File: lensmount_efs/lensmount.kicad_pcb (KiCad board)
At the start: 2 copper layers, 49.8 x 49.8 mm, 39 parts, among them J1 VBAT, J10 Picoblade DNP, J2 DETECT, J3 AGND, J4 VDD, J5 DOUT, J6 DIN, J7 DCLK, J8 DGND, P1 TC2030-CTX-Tag-Connect, Q1 2N7002, Q2 2N7002, Q3 2N7002, Q4 AO3401A, Q5 AO3401A, U1 STM32F042G6Ux, U2 XC6206PxxxMR

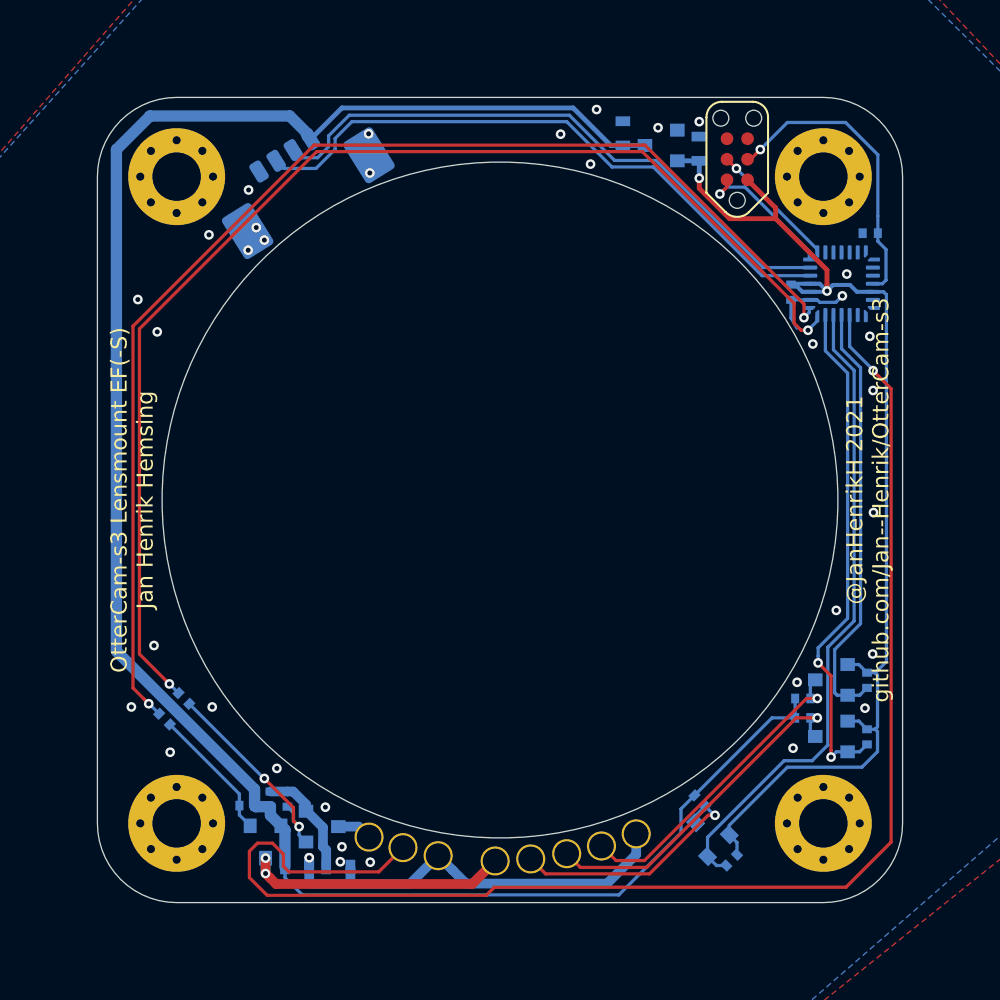
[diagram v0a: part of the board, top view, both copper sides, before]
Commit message: updated to kicad 6
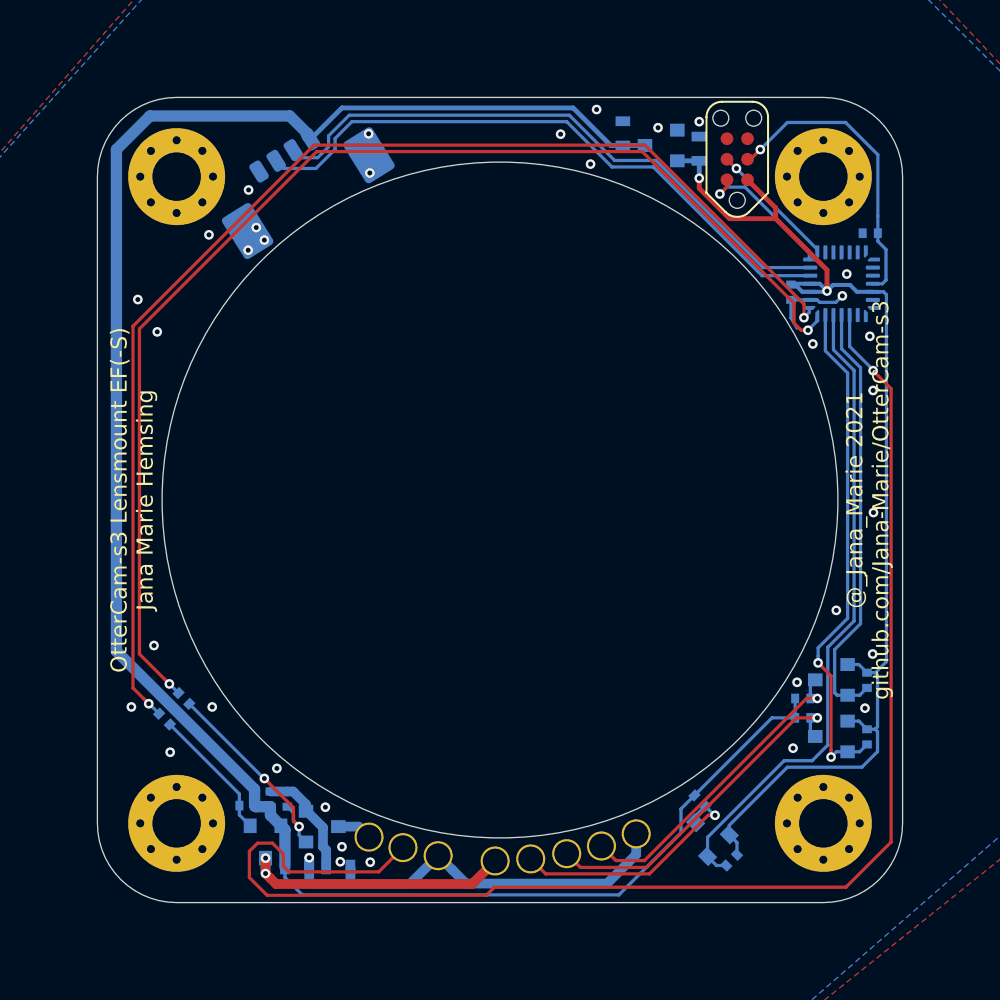
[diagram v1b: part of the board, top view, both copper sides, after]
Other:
- net class Default removed
- board text added: "@_Jana_Marie 2021 github.com/Jana-Marie/OtterCam-s3"
- board text added: "OtterCam-s3 Lensmount EF(-S) Jana Marie Hemsing"
- board text removed: "@JanHenrikH 2021 github.com/Jan--Henrik/OtterCam-s3"
- board text removed: "OtterCam-s3 Lensmount EF(-S) Jan Henrik Hemsing"

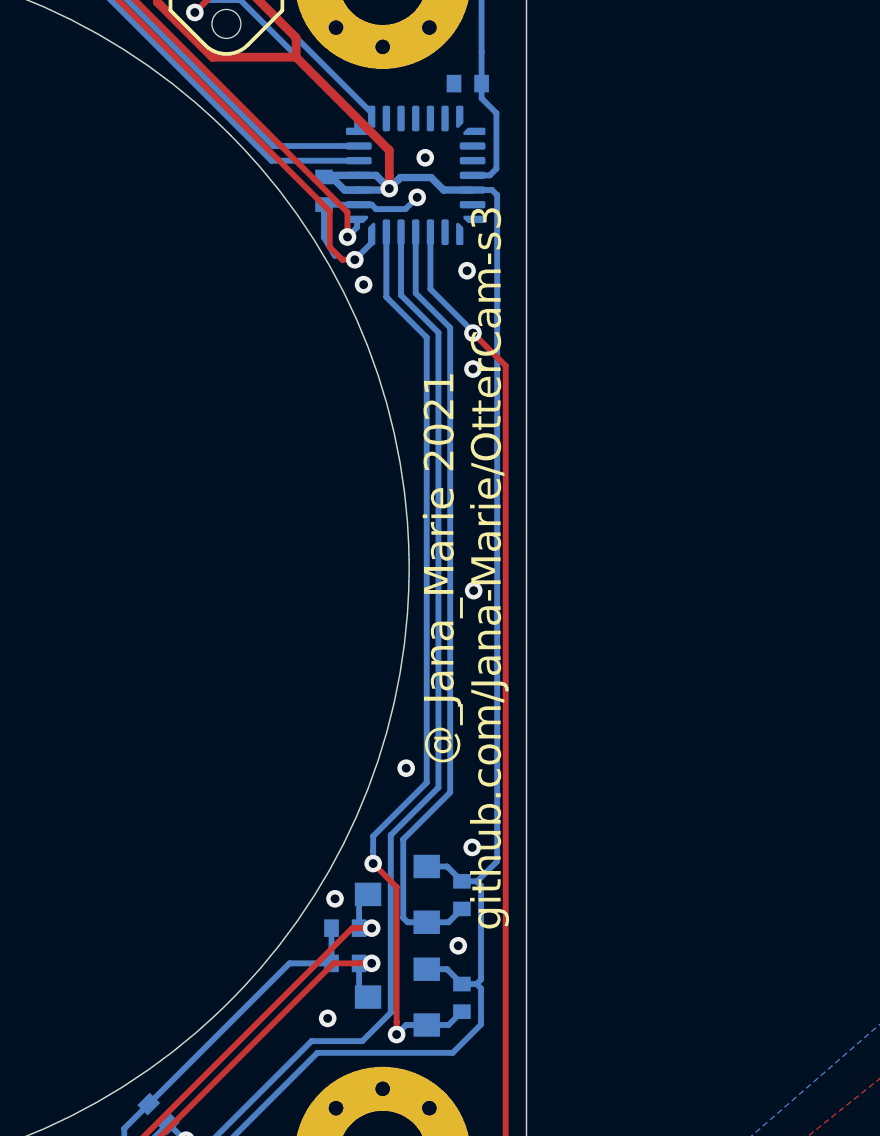
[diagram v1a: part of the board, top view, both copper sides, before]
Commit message: updated lensmount
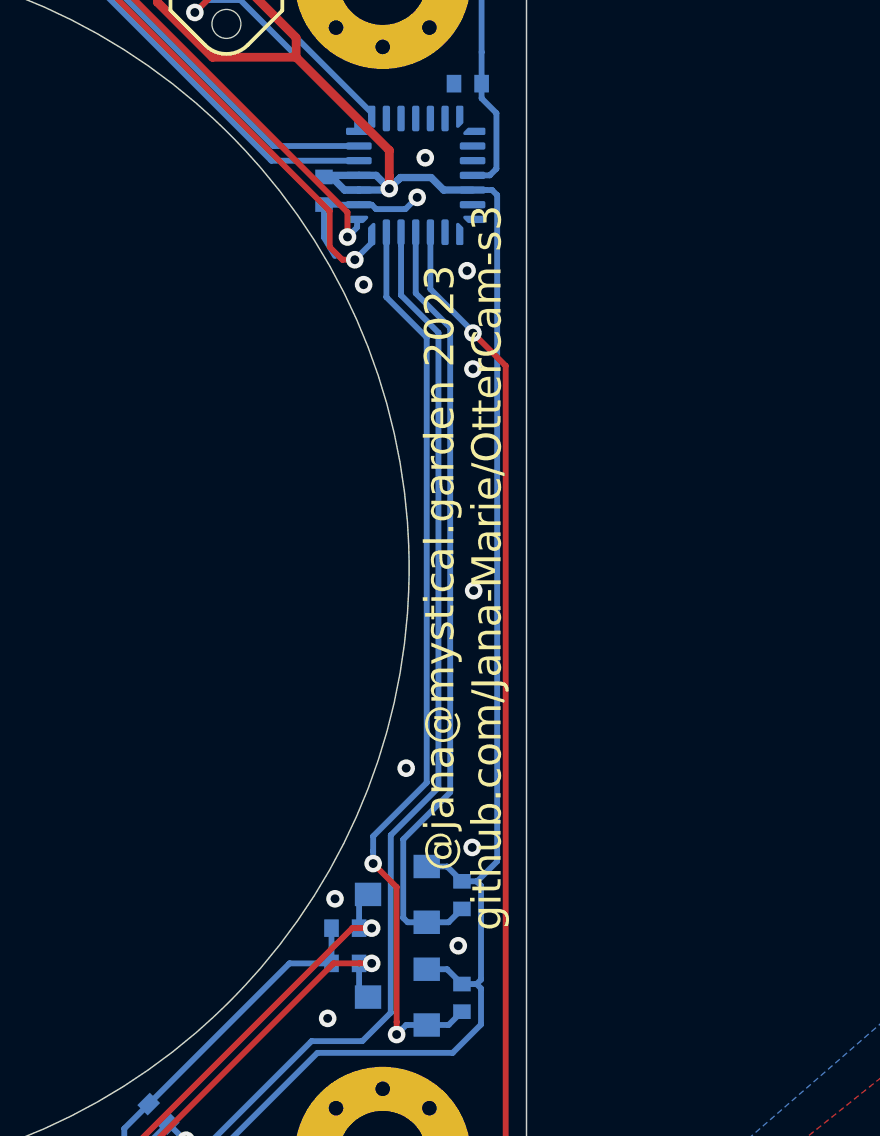
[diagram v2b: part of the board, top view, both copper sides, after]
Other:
- board text added: "@jana@mystical.garden 2023 github.com/Jana-Marie/OtterCam-s3"
- board text removed: "@_Jana_Marie 2021 github.com/Jana-Marie/OtterCam-s3"
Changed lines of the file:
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@@
       (drillshape 0)
       (scaleselection 1)
-      (outputdirectory "gerber/")
+      (outputdirectory "gerber_v1.0.1/")
     )
   )
@@
   (gr_arc (start 120 75.1) (mid 123.464823 76.535177) (end 124.9 80) (layer "Edge.Cuts") (width 0.05))
   (gr_line (start 75.1 80) (end 75.1 120) (layer "Edge.Cuts") (width 0.05))
-  (gr_text "@_Jana_Marie 2021\ngithub.com/Jana-Marie/OtterCam-s3" (at 122.75 100 90) (layer "F.SilkS")
+  (gr_text "@jana@mystical.garden 2023\ngithub.com/Jana-Marie/OtterCam-s3" (at 122.75 100 90) (layer "F.SilkS")
     (effects (font (size 1 1) (thickness 0.15)))
   )
